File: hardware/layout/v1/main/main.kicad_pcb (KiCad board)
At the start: 4 copper layers, 39.8 x 78 mm, 47 parts, among them J1 POWER IN (2P push-in), J2 SENSOR I/O (7P push-in), J3 UI board, J4 RELAY OUT (3P push-in), K1 G6S-2F DC5, Q1 BC847B,215, U1 SCT2400TVBR, U2 LM66100, U3 XIAO ESP32C6

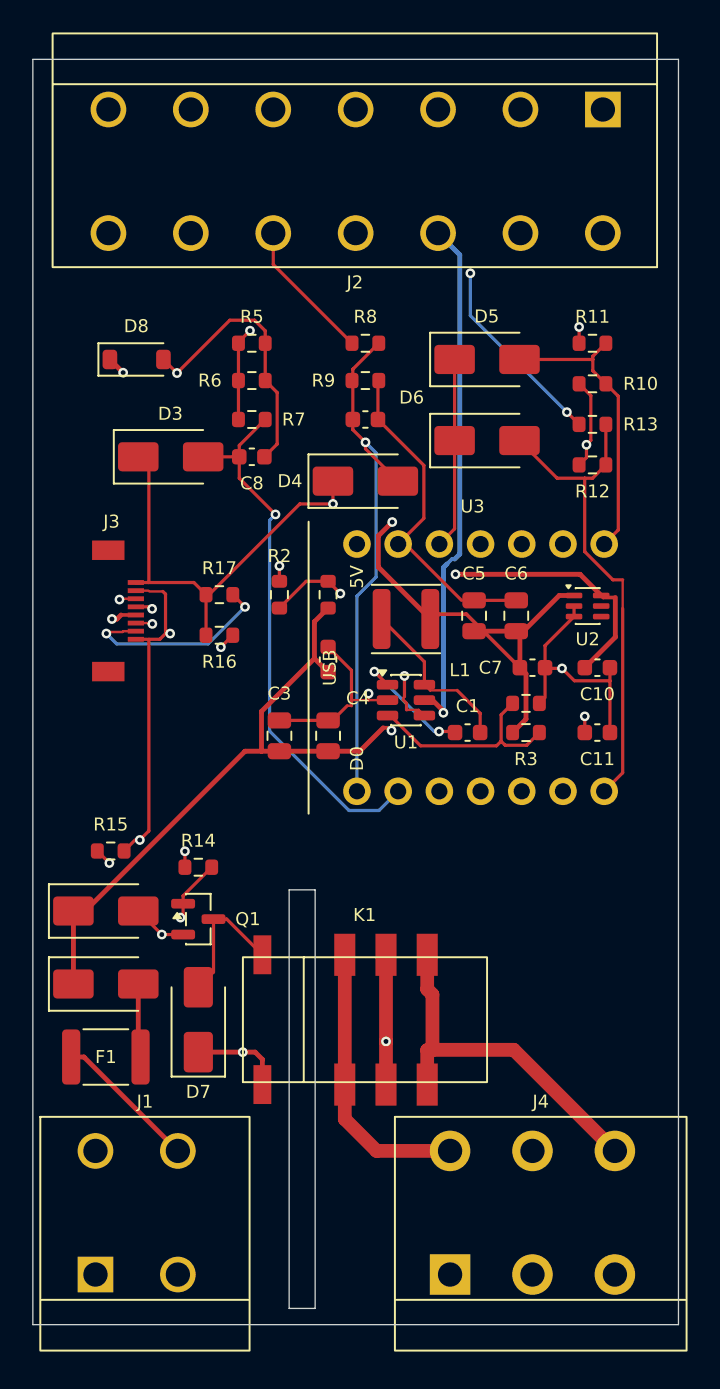
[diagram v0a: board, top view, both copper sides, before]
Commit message: replace SS16 Schottky diodes with SS34
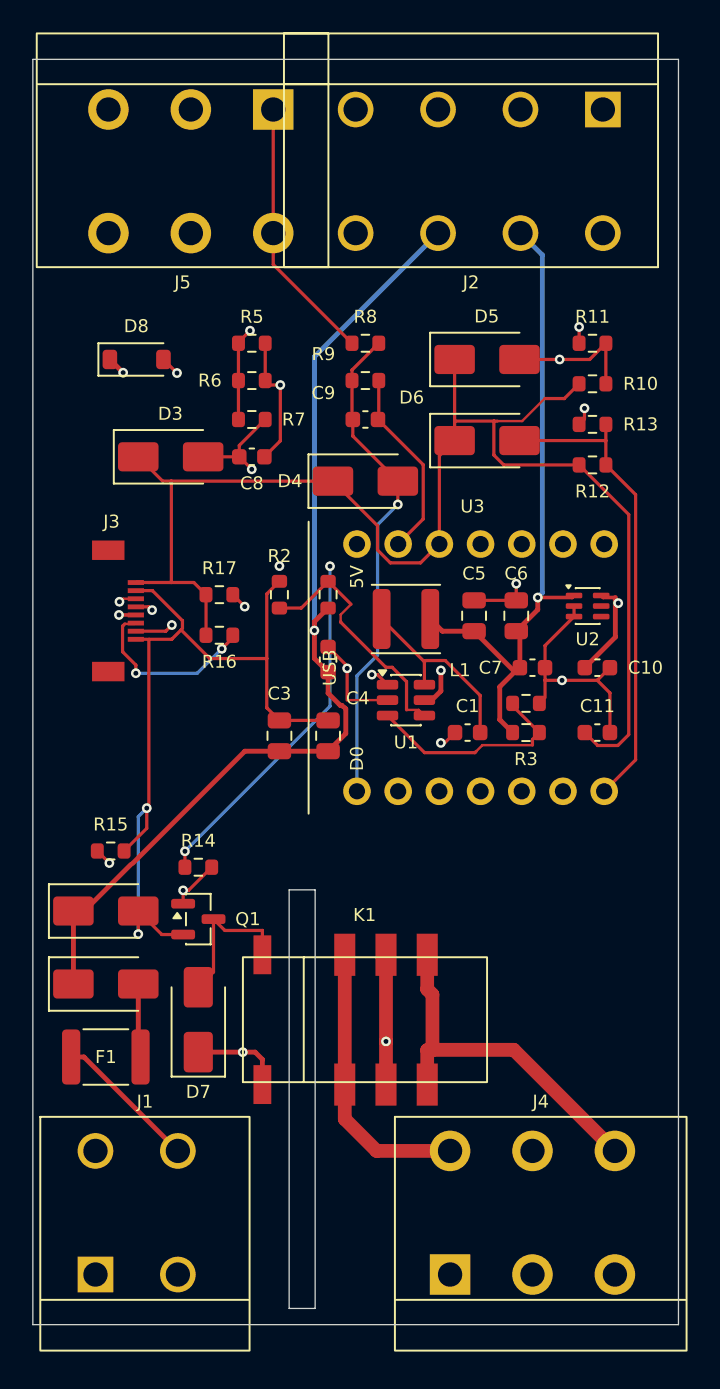
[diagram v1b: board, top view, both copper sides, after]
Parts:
- added J5: KF142R-5.08-3P, gateway_fp:TerminalBlock_Kefa_KF142R-5.08-3P, F.Cu at (9.74, -71.1)
- D2, D3, D4, D5, D6, D7: value SS16 -> SS34
- J1: value POWER IN (2P push-in) -> KF142R-5.08-2P
- J2: value SENSOR I/O (7P push-in) -> KF142R-5.08-4P; footprint gateway_fp:TerminalBlock_Kefa_KF142R-5.08-7P -> gateway_fp:TerminalBlock_Kefa_KF142R-5.08-4P
- J3: value UI board -> FPC-05F-8PH20
- J4: value RELAY OUT (3P push-in) -> KF142R-5.08-3P
- Q1: value BC847B,215 -> MMBT3904
- R1: value 100k 1% -> 100k
- R2: value 20k 1% -> 20k
- R3: value 51k 1% -> 51k
- R4: value 10k 1% -> 10k
- moved J2 7.62 mm to (27.5, -71.1)
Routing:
- net IO2_TERM: track 46.5 -> 66.2 mm, vias 2 -> 1
- net GND: track 86.1 -> 96.3 mm, vias 7 -> 8
- net +3V3: track 78.6 -> 85.2 mm, vias 3 -> 0
- net IO1_TERM: track 46.2 -> 52.2 mm
- net I2C_SCL: track 38.4 -> 32.7 mm
- net MA_MCU: track 33.6 -> 38.6 mm
- net RELAY_MCU: track 44.1 -> 40.7 mm, vias 1 -> 2
- net +24V_LOOP: track 84.1 -> 81.4 mm
- net IO1_MCU: track 18.2 -> 20.8 mm, vias 0 -> 1
- net V0_10_MCU: track 33.0 -> 30.5 mm
- net LED_DATA: track 28.7 -> 26.3 mm
- net I2C_SDA: track 31.5 -> 33.3 mm
- net +5V_XIAO: track 22.4 -> 23.8 mm
- net BUCK5_SW: track 10.5 -> 11.8 mm
- net RELAY_BASE: track 10.7 -> 9.47 mm
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
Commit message: pin PlatformIO to 6.1.19 to avoid ESP8266 build failures in 6.2.0, add xiao_c6 build target to CI workflow with filesystem build step, update README with v1 board hardware details and Docker build instructions, replace SCT2400 with SCT2601 buck converter (4.5-60V input, 700kHz), add external catch diode and update feedback divider for 5.05V output, replace SS16 with SS34/SS36 Schottky diodes, add 50mA PTC fuse to 4-20mA input, reduce shunt from 165R to 120R (20mA = 2.40V), replace single Schottky cl
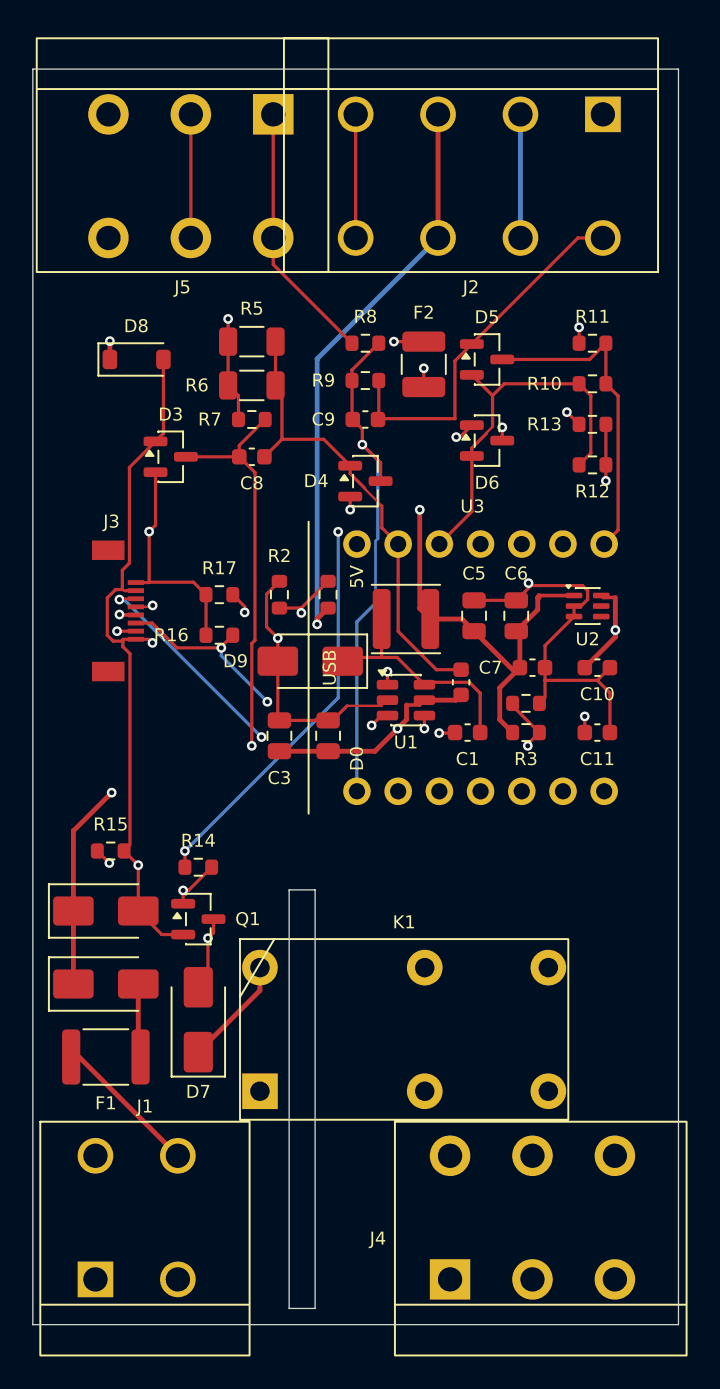
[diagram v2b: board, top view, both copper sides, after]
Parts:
- added D9: SS36, Diode_SMD:D_SMA, F.Cu at (17.1, -40.9)
- added F2: 50mA, Fuse:Fuse_1210_3225Metric, F.Cu at (24.1, -59.2)
- D1: value SMAJ33A -> SMAJ30A
- D2: value SS34 -> SS36
- D3, D4, D5, D6: value SS34 -> BAT54S; footprint Diode_SMD:D_SMA -> Package_TO_SOT_SMD:SOT-23
- K1: value G6S-2F DC5 -> G6B-2114P-US DC5; footprint gateway_fp:Relay_DPDT_Omron_G6S-2F_2A -> gateway_fp:Relay_1A1B_Omron_G6B-2114P
- L1: value 4.7uH -> 22uH; footprint Inductor_SMD:L_APV_ANR4012 -> Inductor_SMD:L_Sunlord_SWPA4020S
- R14: value 1k -> 470R
- R3: value 51k -> 56k
- R5, R6: value 330R -> 240R; footprint Resistor_SMD:R_0603_1608Metric -> Resistor_SMD:R_1206_3216Metric
- U1: value SCT2400TVBR -> SCT2601TVBR
- moved C4 8.32 mm to (26.4, -39.6)
- moved K1 2.46 mm to (22.9, -18.2), turned to 0 degrees
- moved R6 0.30 mm to (13.5, -57.9)
- moved J1 0.30 mm to (6.40, -6.60)
- moved J4 0.30 mm to (30.8, -6.60)
- moved J2 0.30 mm to (27.5, -70.8)
- moved J5 0.30 mm to (9.74, -70.8)
- moved R5 0.10 mm to (13.5, -60.6)
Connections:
- D3 pad 1: +3V3 -> GND
- D3 pad 2: MA_MCU -> +3V3
- D4 pad 1: +3V3 -> GND
- D4 pad 2: V0_10_MCU -> +3V3
- D5 pad 1: +3V3 -> GND
- D5 pad 2: IO1_MCU -> +3V3
- D6 pad 1: +3V3 -> GND
- D6 pad 2: IO2_MCU -> +3V3
- J4 pad 1: RELAY_NC -> RELAY_COM
- J4 pad 2: RELAY_COM -> RELAY_NO
- J4 pad 3: RELAY_NO -> RELAY_NC
- K1 pad 1: +5V -> RELAY_COIL_N
- K1 pad 3: RELAY_NC -> RELAY_COM
- K1 pad 4: RELAY_COM -> RELAY_NO
- K1 pad 5: RELAY_NO -> RELAY_NC
- K1 pad 8: RELAY_NO -> +5V
- R5 pad 1: MA_TERM -> MA_SHUNT
- R6 pad 1: MA_TERM -> MA_SHUNT
- R7 pad 1: MA_TERM -> MA_SHUNT
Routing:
- net GND: track 96.3 -> 132.9 mm, vias 8 -> 5
- net MA_SHUNT: track 0.00 -> 19.1 mm, vias 0 -> 2
- net IO2_TERM: track 66.2 -> 47.8 mm
- net RELAY_NO: track 29.9 -> 12.6 mm
- net IO1_TERM: track 52.2 -> 40.6 mm
- net I2C_SCL: track 32.7 -> 44.2 mm
- net RELAY_COM: track 27.4 -> 19.9 mm, vias 1 -> 0
- net +5V: track 131.2 -> 123.9 mm, vias 4 -> 3
- net LED_DATA: track 26.3 -> 33.5 mm
- net RELAY_COIL_N: track 9.39 -> 15.3 mm, vias 0 -> 1
- net +3V3: track 85.2 -> 79.8 mm, vias 0 -> 3
- net +24V_LOOP: track 81.4 -> 86.6 mm, vias 2 -> 3
- net RELAY_NC: track 25.0 -> 20.9 mm
- net MA_TERM: track 22.4 -> 18.5 mm
- net MA_MCU: track 38.6 -> 35.7 mm
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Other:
- board size 39.8 x 78 mm -> 39.8 x 77.4 mm

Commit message: refactor to multi-sensor firmware
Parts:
- added D10: BAT54S, Package_TO_SOT_SMD:SOT-23, F.Cu at (2.30, -50.6)
- added D11: BAT54S, Package_TO_SOT_SMD:SOT-23, F.Cu at (2.30, -54.4)
- added J6: 2086-1203/700-000/997-605, gateway_fp:TerminalBlock_WAGO_2086-1203_SMD, F.Cu at (6.65, -70.2)
- added R18: 4k7, Resistor_SMD:R_0603_1608Metric, F.Cu at (5.40, -50.3)
- added R19: 330R, Resistor_SMD:R_0603_1608Metric, F.Cu at (5.40, -53.5)
- added R20: 4k7, Resistor_SMD:R_0603_1608Metric, F.Cu at (2.15, -59.4)
- added R21: 330R, Resistor_SMD:R_0603_1608Metric, F.Cu at (2.15, -57.3)
- J2: value KF142R-5.08-4P -> 2086-1204/700-000/997-605; footprint gateway_fp:TerminalBlock_Kefa_KF142R-5.08-4P -> gateway_fp:TerminalBlock_WAGO_2086-1204_SMD
- J5: value KF142R-5.08-3P -> 2086-1203/700-000/997-605; footprint gateway_fp:TerminalBlock_Kefa_KF142R-5.08-3P -> gateway_fp:TerminalBlock_WAGO_2086-1203_SMD
- moved J5 8.29 mm to (18.0, -70.2)
- moved J2 3.64 mm to (31.1, -70.2)
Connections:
- J2 pad 1: GND -> +5V
- J2 pad 2: +5V -> +24V_LOOP
- J2 pad 3: +24V_LOOP -> MA_TERM
- J2 pad 4: MA_TERM -> V0_10_TERM
- J5 pad 1: V0_10_TERM -> IO1_TERM
- J5 pad 2: IO1_TERM -> IO2_TERM
- J5 pad 3: IO2_TERM -> IO3_TERM
- U3 pad 10: (no net) -> IO3_MCU
- U3 pad 11: (no net) -> IO4_MCU
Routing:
- net IO4_MCU: track 0.00 -> 41.6 mm, vias 0 -> 3
- net IO3_MCU: track 0.00 -> 35.9 mm, vias 0 -> 1
- net IO3_TERM: track 0.00 -> 30.4 mm, vias 0 -> 2
- net IO4_TERM: track 0.00 -> 27.3 mm, vias 0 -> 2
- net GND: track 132.9 -> 158.3 mm, vias 5 -> 7
- net +3V3: track 79.8 -> 104.2 mm, vias 3 -> 6
- net +5V: track 123.9 -> 145.7 mm, vias 3 -> 5
- net IO2_TERM: track 47.8 -> 32.6 mm, vias 1 -> 2
- net IO1_TERM: track 40.6 -> 28.3 mm, vias 1 -> 2
- net +24V_LOOP: track 86.6 -> 95.6 mm, vias 3 -> 6
- net I2C_SDA: track 31.5 -> 36.9 mm, vias 2 -> 1
- net LED_DATA: track 33.5 -> 28.7 mm
- net IO1_MCU: track 19.9 -> 24.5 mm, vias 0 -> 1
- net BTN_LADDER: track 25.7 -> 29.5 mm, vias 2 -> 1
- net I2C_SCL: track 44.2 -> 40.6 mm
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
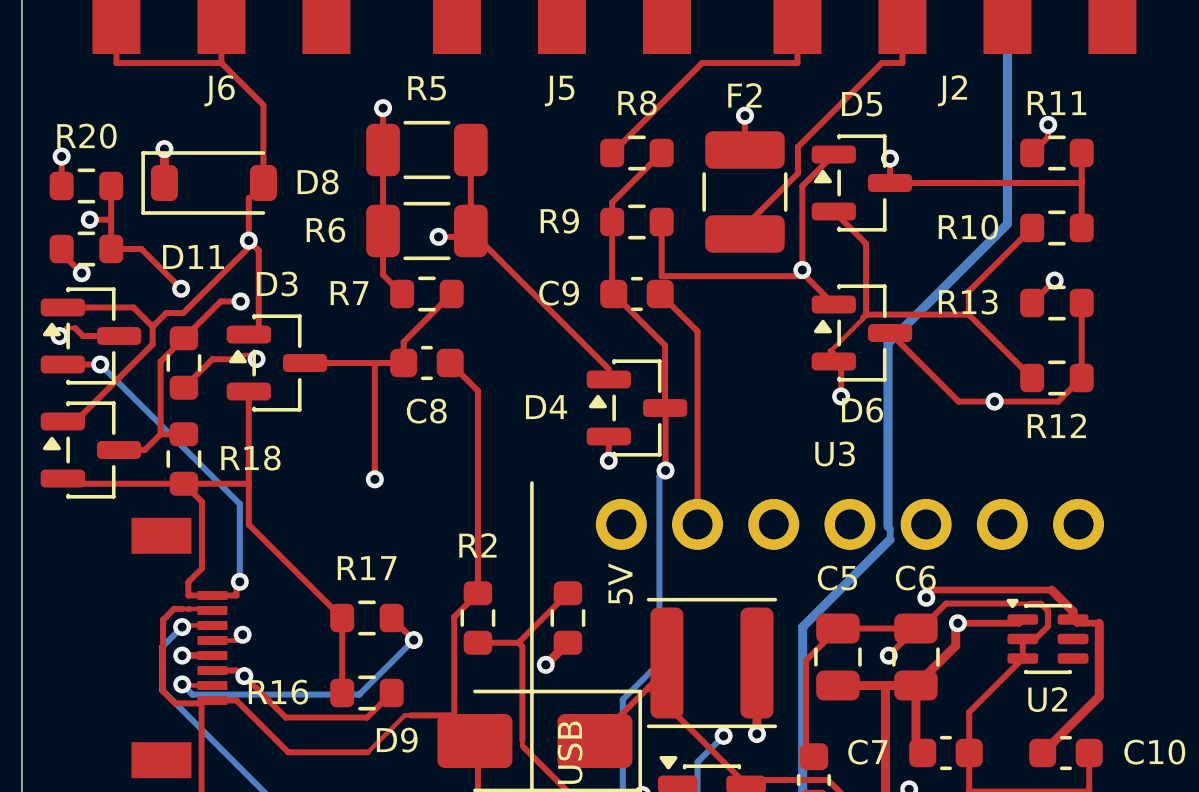
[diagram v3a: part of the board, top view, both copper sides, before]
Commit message: extend GND track joints on main board to fully seat on pads/vias
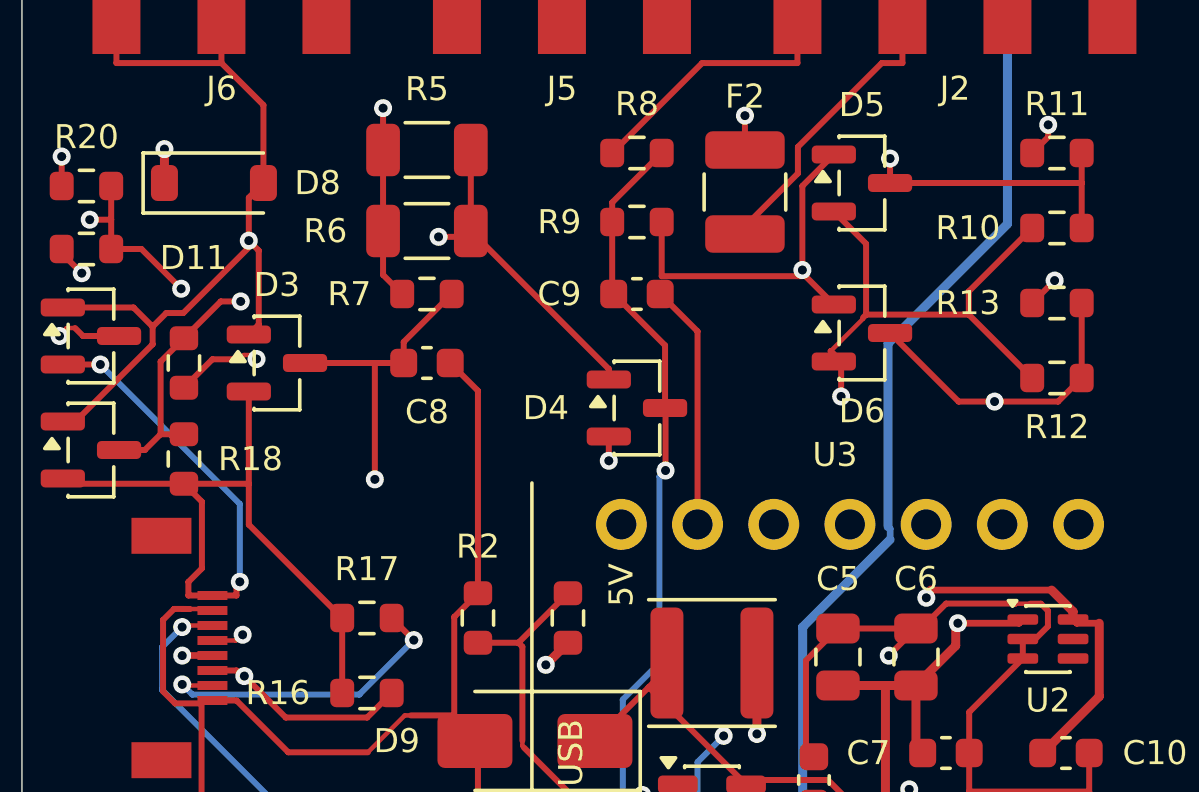
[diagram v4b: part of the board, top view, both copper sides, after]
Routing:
- net GND: track 158.3 -> 160.1 mm
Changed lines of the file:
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@@
+	)
+	(segment
+		(start 19.5625 -53.3)
+		(end 19.5625 -52.95)
+		(width 0.2)
+		(layer "F.Cu")
+		(net "GND")
 	)
 	(segment
@@
 	)
 	(segment
+		(start 5.3686 -45.302)
+		(end 5.5292 -45.2998)
+		(width 0.2)
+		(layer "F.Cu")
+		(net "GND")
+	)
+	(segment
 		(start 4.8112 -55.1662)
 		(end 4.3563 -54.7113)
@@
 	)
 	(segment
+		(start 7.5625 -59.0125)
+		(end 8.05 -59.5)
+		(width 0.2)
+		(layer "F.Cu")
+		(net "GND")
+	)
+	(segment
 		(start 33.9655 -45.4767)
 		(end 34.2 -45.2422)
@@
 	)
 	(segment
+		(start 5.5292 -45.2998)
+		(end 5.5906 -45.2998)
+		(width 0.2)
+		(layer "F.Cu")
+		(net "GND")
+	)
+	(segment
 		(start 33.3625 -44.3)
 		(end 33.3625 -43.65)
@@
 	)
 	(segment
+		(start 7.894 -54.7815)
+		(end 7.5625 -54.45)
+		(width 0.2)
+		(layer "F.Cu")
+		(net "GND")
+	)
+	(segment
 		(start 31.575 -40.5)
 		(end 31.575 -39.2135)
@@
 		(start 4.7041 -42.5532)
 		(end 5.1032 -42.1541)
+		(width 0.2)
+		(layer "F.Cu")
+		(net "GND")
+	)
+	(segment
+		(start 33.1153 -45.4808)
+		(end 33.1194 -45.4767)
 		(width 0.2)
 		(layer "F.Cu")
@@
 		(layer "F.Cu")
 		(net "GND")
+	)
+	(segment
+		(start 33.1194 -45.4767)
+		(end 33.1153 -45.4808)
+		(width 0.15)
+		(layer "F.Cu")
+		(net "GND")
